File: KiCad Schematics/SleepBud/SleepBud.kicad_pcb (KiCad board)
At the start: 2 copper layers, 155 x 55 mm, 87 parts, among them J1 USB_B_Micro, J2 12V Barrel Jack, Q1 AO3400A, Q2 FQP27P06, SW1 Mode Button, SW2 Up Button, SW3 Down Button, SW4 EN Button, SW5 Switch Button, SW6 Reset Button, U1 ESP32-S3-WROOM-1, U2 DS3231SN_, U3 PIR, U4 AMS1117-3.3, U5 AMS1117-5.0, U6 TXS0108EPW, U7 Lamp SMD

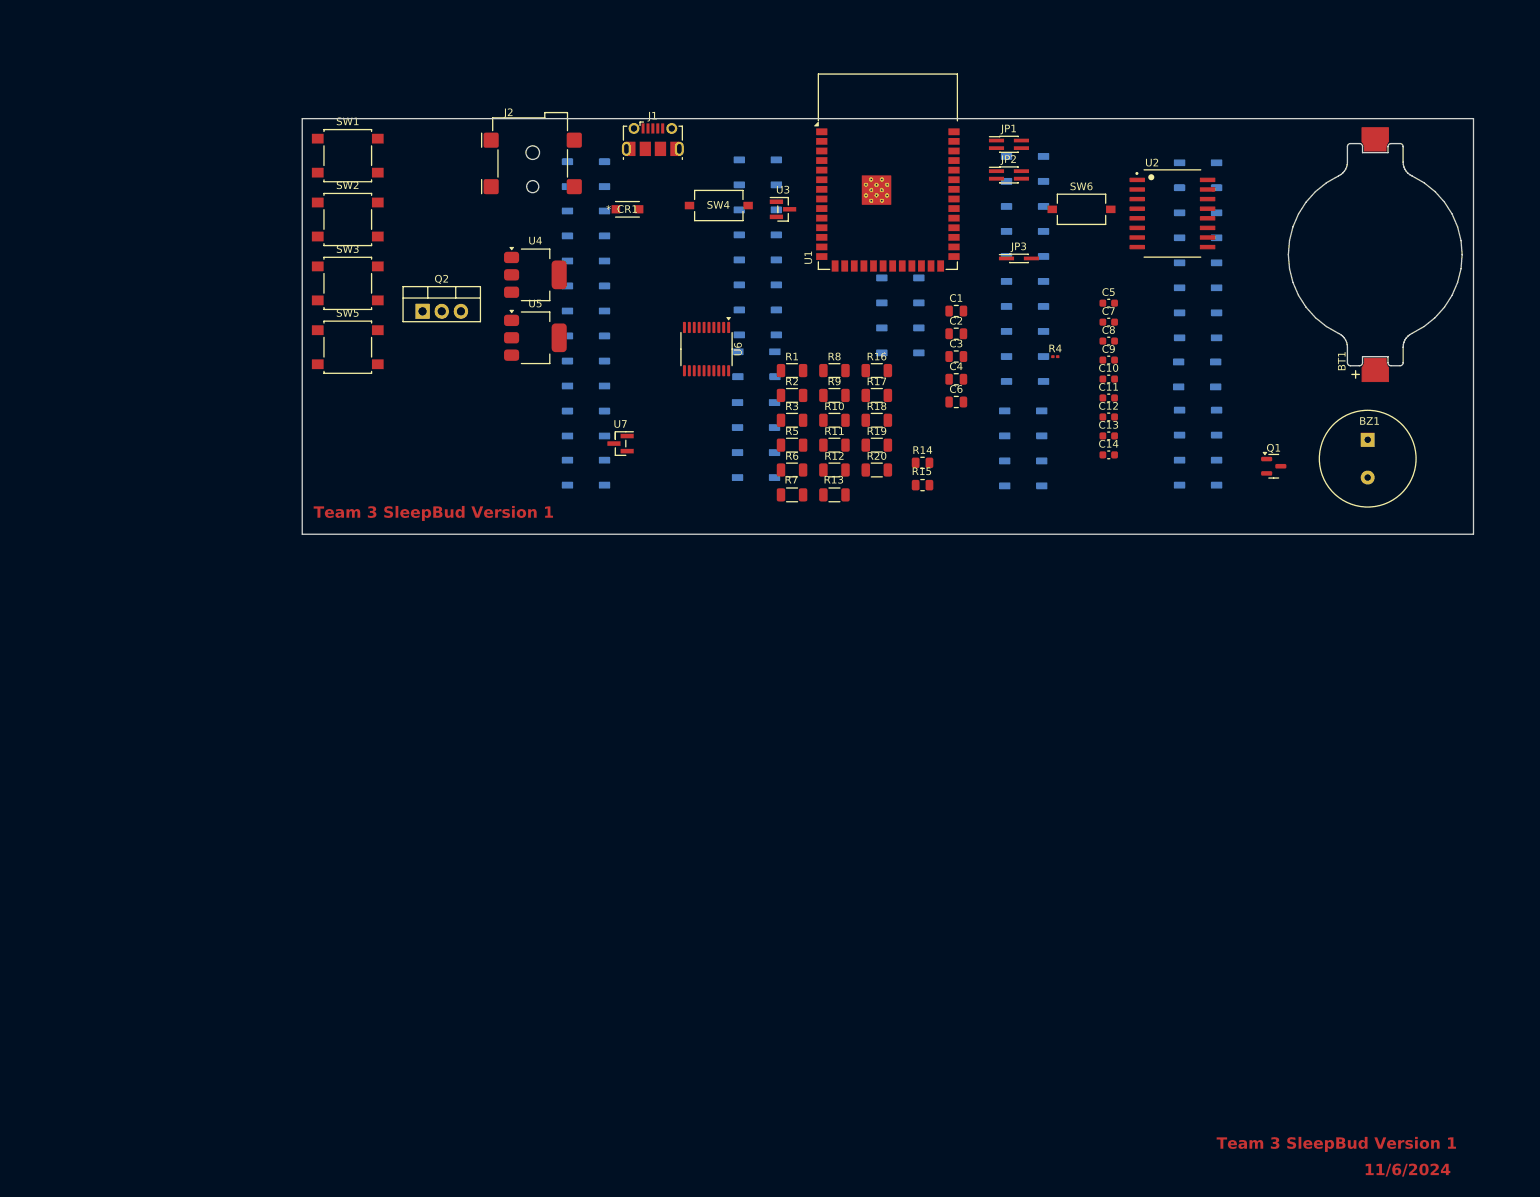
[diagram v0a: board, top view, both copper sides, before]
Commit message: Switched some footprints and schematics
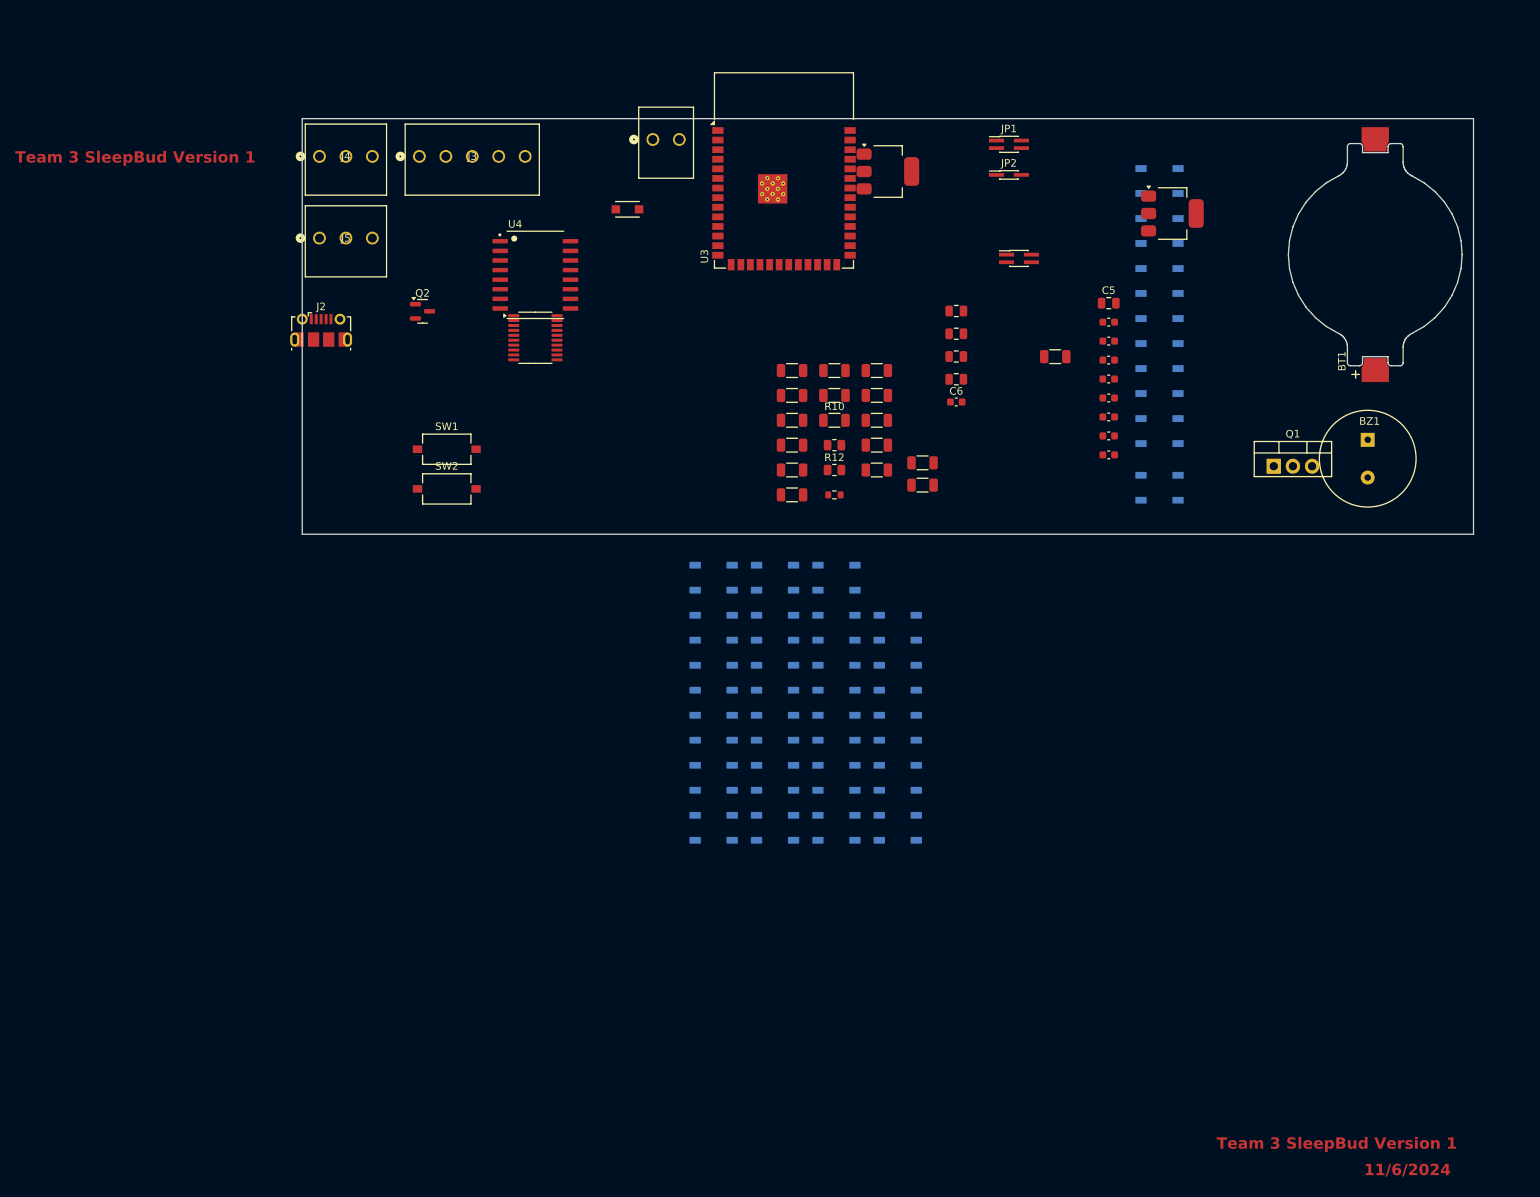
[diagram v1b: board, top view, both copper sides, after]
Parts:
- removed D31: WS2812B, LED_SMD:LED_WS2812B_PLCC4_5.0x5.0mm_P3.2mm
- removed SW3: Down Button, Button_Switch_SMD:SW_SPST_B3S-1000
- removed SW4: EN Button, Button_Switch_SMD:SW_Tactile_SPST_NO_Straight_CK_PTS636Sx25SMTRLFS
- removed SW5: Switch Button, Button_Switch_SMD:SW_SPST_B3S-1000
- removed SW6: Reset Button, Button_Switch_SMD:SW_Tactile_SPST_NO_Straight_CK_PTS636Sx25SMTRLFS
- removed U6: TXS0108EPW, Package_SO:TSSOP-20_4.4x6.5mm_P0.65mm
- removed U7: Lamp SMD, Connector_PinHeader_1.00mm:PinHeader_1x03_P1.00mm_Vertical_SMD_Pin1Right
- added D1: WS2812B, LED_SMD:LED_WS2812B_PLCC4_5.0x5.0mm_P3.2mm, B.Cu at (179.4, 62.2)
- added J3: 1984798, 1984798:CONN_1984798_PXC, F.Cu at (81.5, 59.0)
- added J4: 1984772, 1984772:CONN_1984772_PXC, F.Cu at (68.3, 59.0)
- added J5: 1984772, 1984772:CONN_1984772_PXC, F.Cu at (68.3, 69.8)
- C10: value 0.1uF -> 22pF
- C5: value 1uF -> 22uF; footprint Capacitor_SMD:C_0603_1608Metric -> Capacitor_SMD:C_0805_2012Metric
- C6: value 22uF -> 0.1uF; footprint Capacitor_SMD:C_0805_2012Metric -> Capacitor_SMD:C_0603_1608Metric
- C7: value 0.1uF -> 1uF
- C8: value 22pF -> 0.1uF
- J1: value USB_B_Micro -> 12V Barrel Jack; footprint Connector_USB:USB_Micro-B_Molex-105017-0001 -> 1984769:CONN_1984769_PXC
- J2: value 12V Barrel Jack -> USB_B_Micro; footprint Connector_BarrelJack:BarrelJack_Wuerth_694108106102_2.5x5.5mm -> Connector_USB:USB_Micro-B_Molex-105017-0001
- JP2: value JTAG -> Boot Option; footprint Connector_PinHeader_1.00mm:PinHeader_2x02_P1.00mm_Vertical_SMD -> Connector_PinHeader_1.00mm:PinHeader_2x01_P1.00mm_Vertical_SMD
- JP3: value Boot Option -> JTAG; footprint Connector_PinHeader_1.00mm:PinHeader_2x01_P1.00mm_Vertical_SMD -> Connector_PinHeader_1.00mm:PinHeader_2x02_P1.00mm_Vertical_SMD
- Q1: value AO3400A -> FQP27P06; footprint Package_TO_SOT_SMD:SOT-23 -> Package_TO_SOT_THT:TO-220-3_Vertical
- Q2: value FQP27P06 -> AO3400A; footprint Package_TO_SOT_THT:TO-220-3_Vertical -> Package_TO_SOT_SMD:SOT-23
- R10, R2, R9: value 470 -> 10k
- R11, R12: value 470 -> 3.3k; footprint Resistor_SMD:R_1206_3216Metric -> Resistor_SMD:R_0805_2012Metric
- R13: value 470 -> 4.7k; footprint Resistor_SMD:R_1206_3216Metric -> Resistor_SMD:R_0603_1608Metric
- R14: value 3.3k -> 10kOhm; footprint Resistor_SMD:R_0805_2012Metric -> Resistor_SMD:R_1206_3216Metric
- R15: value 3.3k -> 470; footprint Resistor_SMD:R_0805_2012Metric -> Resistor_SMD:R_1206_3216Metric
- R16, R17, R18, R19, R20: value 10k -> 470
- R4: value 4.7k -> 10k; footprint Resistor_SMD:R_0201_0603Metric -> Resistor_SMD:R_1206_3216Metric
- R5: value 10k -> 0
- R6, R7: value 0 -> 10k
- R8: value 10kOhm -> 0
- SW1: value Mode Button -> EN Button; footprint Button_Switch_SMD:SW_SPST_B3S-1000 -> Button_Switch_SMD:SW_Tactile_SPST_NO_Straight_CK_PTS636Sx25SMTRLFS
- SW2: value Up Button -> Reset Button; footprint Button_Switch_SMD:SW_SPST_B3S-1000 -> Button_Switch_SMD:SW_Tactile_SPST_NO_Straight_CK_PTS636Sx25SMTRLFS
- U1: value ESP32-S3-WROOM-1 -> AMS1117-3.3; footprint RF_Module:ESP32-S3-WROOM-1 -> Package_TO_SOT_SMD:SOT-223-3_TabPin2
- U2: value DS3231SN_ -> AMS1117-5.0; footprint DS3231SN_:SOIC127P1032X265-16N -> Package_TO_SOT_SMD:SOT-223-3_TabPin2
- U3: value PIR -> ESP32-S3-WROOM-1; footprint Connector_PinHeader_1.00mm:PinHeader_1x03_P1.00mm_Vertical_SMD_Pin1Left -> RF_Module:ESP32-S3-WROOM-1
- U4: value AMS1117-3.3 -> DS3231SN_; footprint Package_TO_SOT_SMD:SOT-223-3_TabPin2 -> DS3231SN_:SOIC127P1032X265-16N
- U5: value AMS1117-5.0 -> TXS0108EPW; footprint Package_TO_SOT_SMD:SOT-223-3_TabPin2 -> Package_SO:TSSOP-20_4.4x6.5mm_P0.65mm
- moved D18 93.0 mm to (136.7, 147.8)
- moved D17 93.0 mm to (136.7, 141.2)
- moved D12 90.0 mm to (144.8, 147.8)
- moved D24 77.5 mm to (128.6, 147.8)
- moved D20 68.8 mm to (128.6, 121.4)
- moved D19 68.8 mm to (128.6, 114.8)
- moved D21 68.8 mm to (128.6, 128.0)
- moved D7 67.6 mm to (179.4, 102.8)
- moved D25 65.6 mm to (120.5, 114.8)
- moved D22 60.2 mm to (128.6, 134.6)
- moved D23 60.2 mm to (128.6, 141.2)
- moved D11 57.8 mm to (144.8, 141.2)
- moved D10 56.7 mm to (144.8, 134.6)
- moved D8 56.7 mm to (144.8, 121.4)
- moved D9 56.7 mm to (144.8, 128.0)
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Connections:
- BZ1 pad 2: Net-(Q1-D) -> Net-(Q2-D)
- C1 pad 1: Net-(Q2-S) -> Net-(Q1-S)
- C10 pad 1: +3.3V -> Net-(J2-D+)
- C11 pad 1: +5V -> +3.3V
- C12 pad 1: GND -> Net-(BT1-+)
- C12 pad 2: Net-(C12-Pad2) -> GND
- C13 pad 1: Net-(BT1-+) -> +3.3V
- C14 pad 1: +3.3V -> +5V
- C5 pad 1: GND -> +3.3V
- C5 pad 2: Net-(U1-EN) -> GND
- C7 pad 1: +3.3V -> GND
- C7 pad 2: GND -> Net-(U3-EN)
- C8 pad 1: Net-(J1-D-) -> GND
- C8 pad 2: GND -> Net-(C8-Pad2)
- C9 pad 1: Net-(J1-D+) -> Net-(J2-D-)
- CR1 pad 1: Net-(Q2-S) -> Net-(Q1-S)
- D12 pad 4: Net-(D12-DIN) -> Net-(D11-DOUT)
- D14 pad 2: Net-(D14-DOUT) -> unconnected-(D14-DOUT-Pad2)
- D15 pad 4: Net-(D14-DOUT) -> Net-(D15-DIN)
- D16 pad 2: Net-(D16-DOUT) -> unconnected-(D16-DOUT-Pad2)
- D2 pad 4: Net-(D2-DIN) -> Net-(D1-DOUT)
- D22 pad 4: Net-(D22-DIN) -> Net-(D21-DOUT)
- D24 pad 4: Net-(D21-DOUT) -> Net-(D24-DIN)
- D25 pad 2: unconnected-(D25-DOUT-Pad2) -> Net-(D25-DOUT)
- D26 pad 4: Net-(D26-DIN) -> Net-(D25-DOUT)
- D27 pad 2: unconnected-(D27-DOUT-Pad2) -> Net-(D27-DOUT)
- D28 pad 4: Net-(D11-DOUT) -> Net-(D27-DOUT)
- D29 pad 2: unconnected-(D29-DOUT-Pad2) -> Net-(D29-DOUT)
- D30 pad 2: Net-(D30-DOUT) -> unconnected-(D30-DOUT-Pad2)
- D30 pad 4: Net-(D16-DOUT) -> Net-(D29-DOUT)
- D6 pad 2: Net-(D26-DIN) -> Net-(D6-DOUT)
- D7 pad 2: Net-(D7-DOUT) -> unconnected-(D7-DOUT-Pad2)
- D7 pad 4: Net-(D7-DIN) -> Net-(D6-DOUT)
- D8 pad 4: Net-(D7-DOUT) -> Net-(D8-DIN)
- J1 pad 1: VBUS -> +12V
- J1 pad 2: Net-(J1-D-) -> GND
- J2 pad 1: +12V -> VBUS
- J2 pad 2: GND -> Net-(J2-D-)
- J2 pad 3: (no net) -> Net-(J2-D+)
- JP2 pad 1: Net-(JP2-TMS) -> Net-(JP2-Input)
- JP2 pad 2: Net-(JP2-TDI) -> GND
- JP3 pad 1: Net-(JP3-Input) -> Net-(JP3-TMS)
- JP3 pad 2: GND -> Net-(JP3-TDI)
- Q1 pad 1: Net-(Q1-G) -> VBUS
- Q1 pad 2: GND -> +12V
- Q1 pad 3: Net-(Q1-D) -> Net-(Q1-S)
- Q2 pad 1: VBUS -> Net-(Q2-G)
- Q2 pad 2: +12V -> GND
- Q2 pad 3: Net-(Q2-S) -> Net-(Q2-D)
- R10 pad 1: /Digit 3 -> +3.3V
- R10 pad 2: Net-(D7-DIN) -> Net-(U3-IO7)
- R11 pad 1: /Digit 4 -> +3.3V
- R11 pad 2: Net-(D12-DIN) -> Net-(U3-IO35)
- R12 pad 1: /Digit 1 -> +3.3V
- R12 pad 2: Net-(D17-DIN) -> Net-(U3-IO36)
- R13 pad 1: /Colon -> +3.3V
- R13 pad 2: Net-(D22-DIN) -> Net-(U3-IO37)
- R14 pad 1: +3.3V -> Net-(U3-IO38)
- R14 pad 2: Net-(U1-IO35) -> GND
- R15 pad 1: +3.3V -> Net-(U5-B1)
- R15 pad 2: Net-(U1-IO36) -> Net-(J5-Pad2)
- R16 pad 1: /Buzzer -> /Digit 1
- R16 pad 2: Net-(Q1-G) -> Net-(D1-DIN)
- R17 pad 1: +3.3V -> /Digit 2
- R17 pad 2: Net-(U1-IO4) -> Net-(D8-DIN)
- R18 pad 1: +3.3V -> /Colon
- R18 pad 2: Net-(U1-IO5) -> Net-(D15-DIN)
- R19 pad 1: +3.3V -> /Digit 3
- R19 pad 2: Net-(U1-IO6) -> Net-(D17-DIN)
- R2 pad 1: /LED Lamp -> +3.3V
- R2 pad 2: Net-(U7-DIN) -> Net-(U3-EN)
- R20 pad 1: +3.3V -> /Digit 4
- R20 pad 2: Net-(U1-IO7) -> Net-(D24-DIN)
- R3 pad 1: Net-(C12-Pad2) -> Net-(C8-Pad2)
- R3 pad 2: Net-(U1-EN) -> Net-(U3-EN)
- R4 pad 1: +3.3V -> /Buzzer
- R4 pad 2: Net-(U1-IO37) -> Net-(Q2-G)
- R5 pad 1: +3.3V -> Net-(U3-IO19)
- R5 pad 2: Net-(U1-EN) -> Net-(J2-D-)
- R6 pad 1: Net-(U1-IO19) -> +3.3V
- R6 pad 2: Net-(J1-D-) -> Net-(U3-IO4)
- R7 pad 1: Net-(U1-IO20) -> +3.3V
- R7 pad 2: Net-(J1-D+) -> Net-(U3-IO5)
- R8 pad 1: Net-(U1-IO38) -> Net-(U3-IO20)
- R8 pad 2: GND -> Net-(J2-D+)
- R9 pad 1: /Digit 2 -> +3.3V
- R9 pad 2: Net-(D2-DIN) -> Net-(U3-IO6)
- SW1 pad 2: Net-(U1-IO4) -> Net-(C8-Pad2)
- SW2 pad 2: Net-(U1-IO5) -> Net-(U4-~{RST})
- U1 pad 3: Net-(U1-EN) -> Net-(Q1-S)
- U2 pad 1: unconnected-(U2-32KHZ-Pad1) -> GND
- U2 pad 2: +3.3V -> +5V
- U2 pad 3: Net-(U1-IO37) -> +12V
- U3 pad 1: +3.3V -> GND
- U3 pad 2: Net-(U1-IO8) -> +3.3V
- U3 pad 3: GND -> Net-(U3-EN)
- U4 pad 1: GND -> unconnected-(U4-32KHZ-Pad1)
- U4 pad 3: Net-(Q2-S) -> Net-(U3-IO37)
- U5 pad 1: GND -> Net-(U3-IO14)
- U5 pad 2: +5V -> +3.3V
- U5 pad 3: +12V -> Net-(U3-IO13)

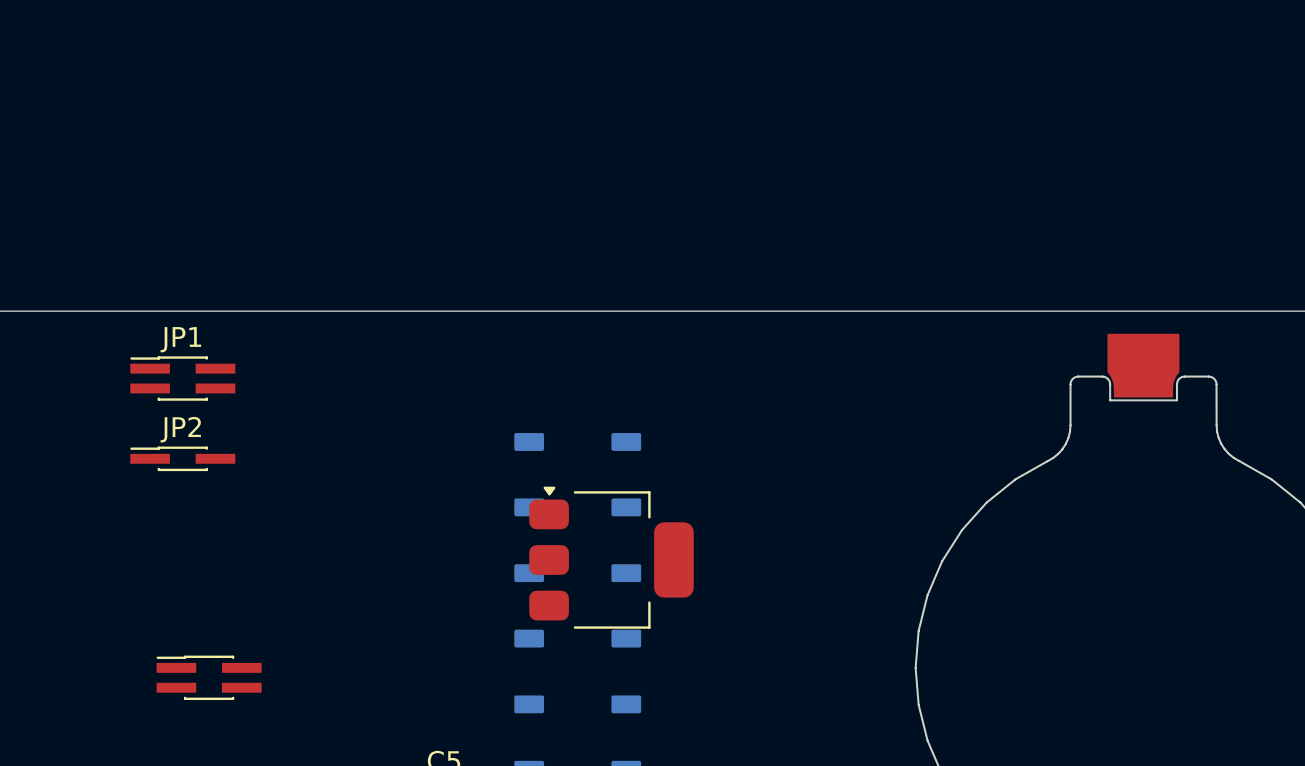
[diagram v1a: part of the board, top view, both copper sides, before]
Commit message: Updated Footprints
Footprint for WB2812B LED was personalized
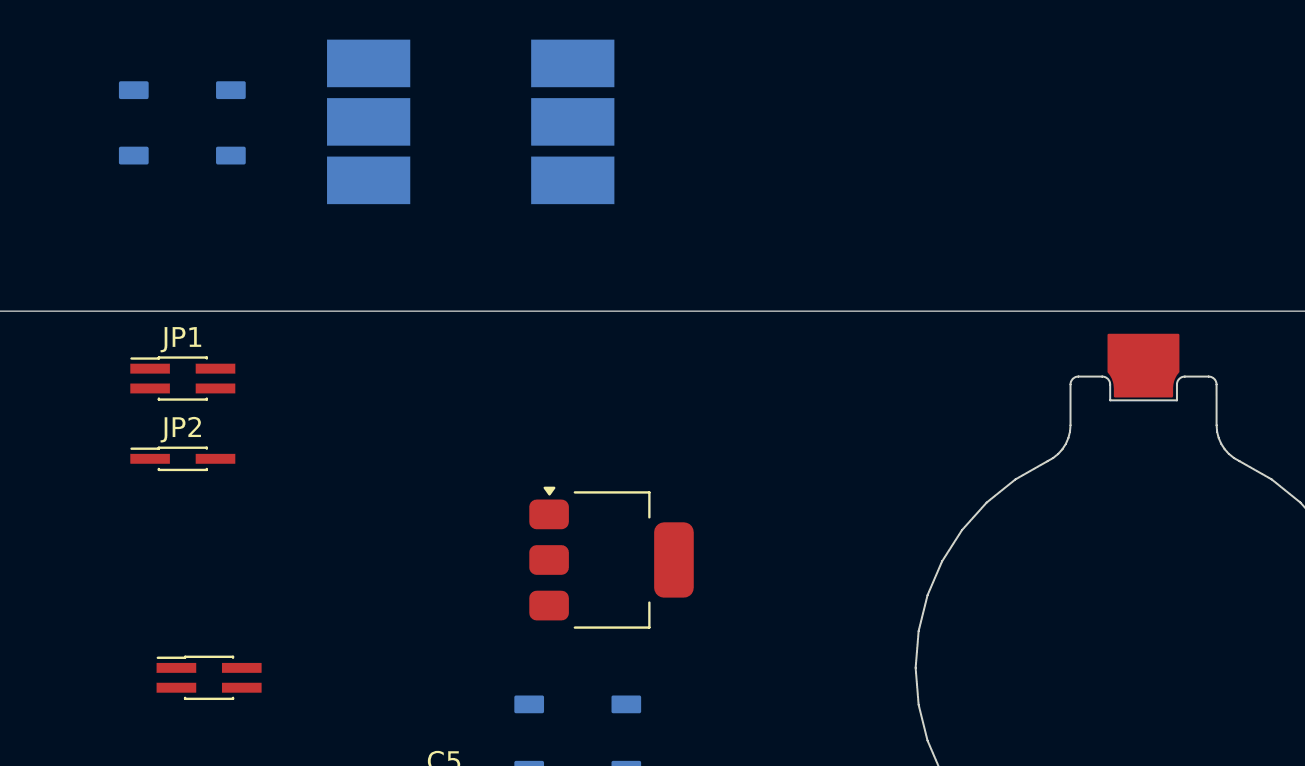
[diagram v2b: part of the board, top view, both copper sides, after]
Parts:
- D1: footprint LED_SMD:LED_WS2812B_PLCC4_5.0x5.0mm_P3.2mm -> Custom:WB2812B
- moved D2 31.5 mm to (159.5, 44.5)
- moved D1 18.6 mm to (174.1, 44.5)
